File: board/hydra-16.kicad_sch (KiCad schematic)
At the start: 35 parts, among them J1 Conn_01x32, J2 Conn_01x24, J3 DE9_Plug, U1 74F573, U2 74F541, U3 AT28C64B, U4 W65C02SxP, U5 6522, U6 6551, U7 MAX232, U8 628512_DIP32, U9 74LS154

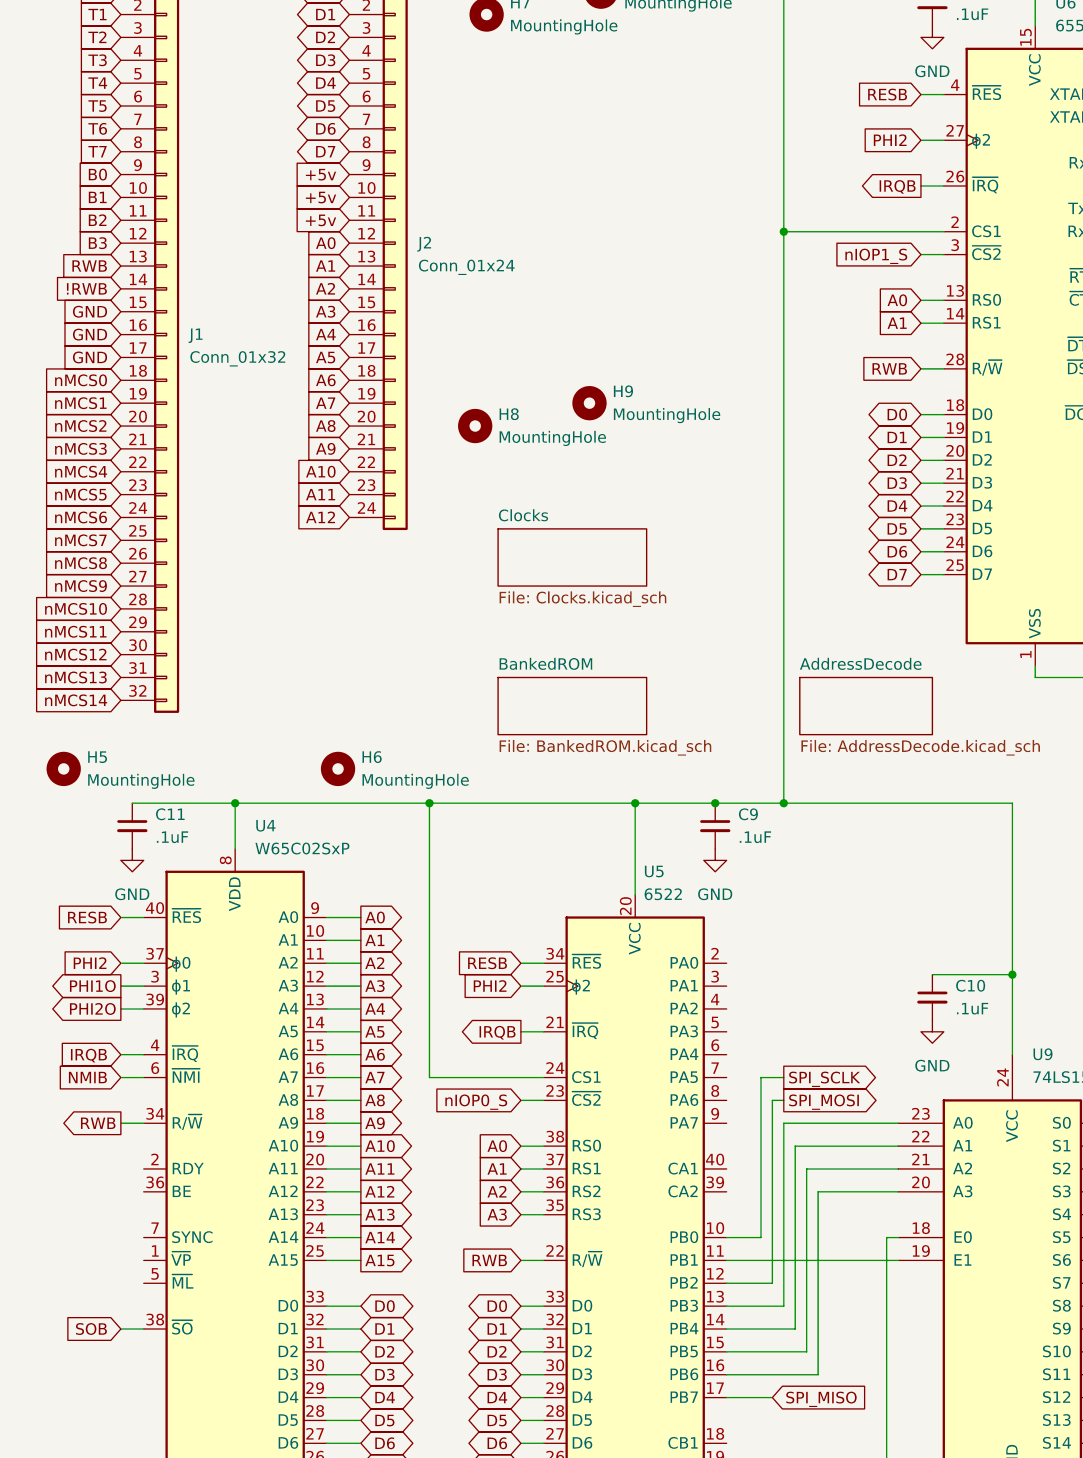
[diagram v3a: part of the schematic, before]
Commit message: Changing to ATX-sized motherboard with 8 62-pin ISA slots.  Other component connection cleanup as well.
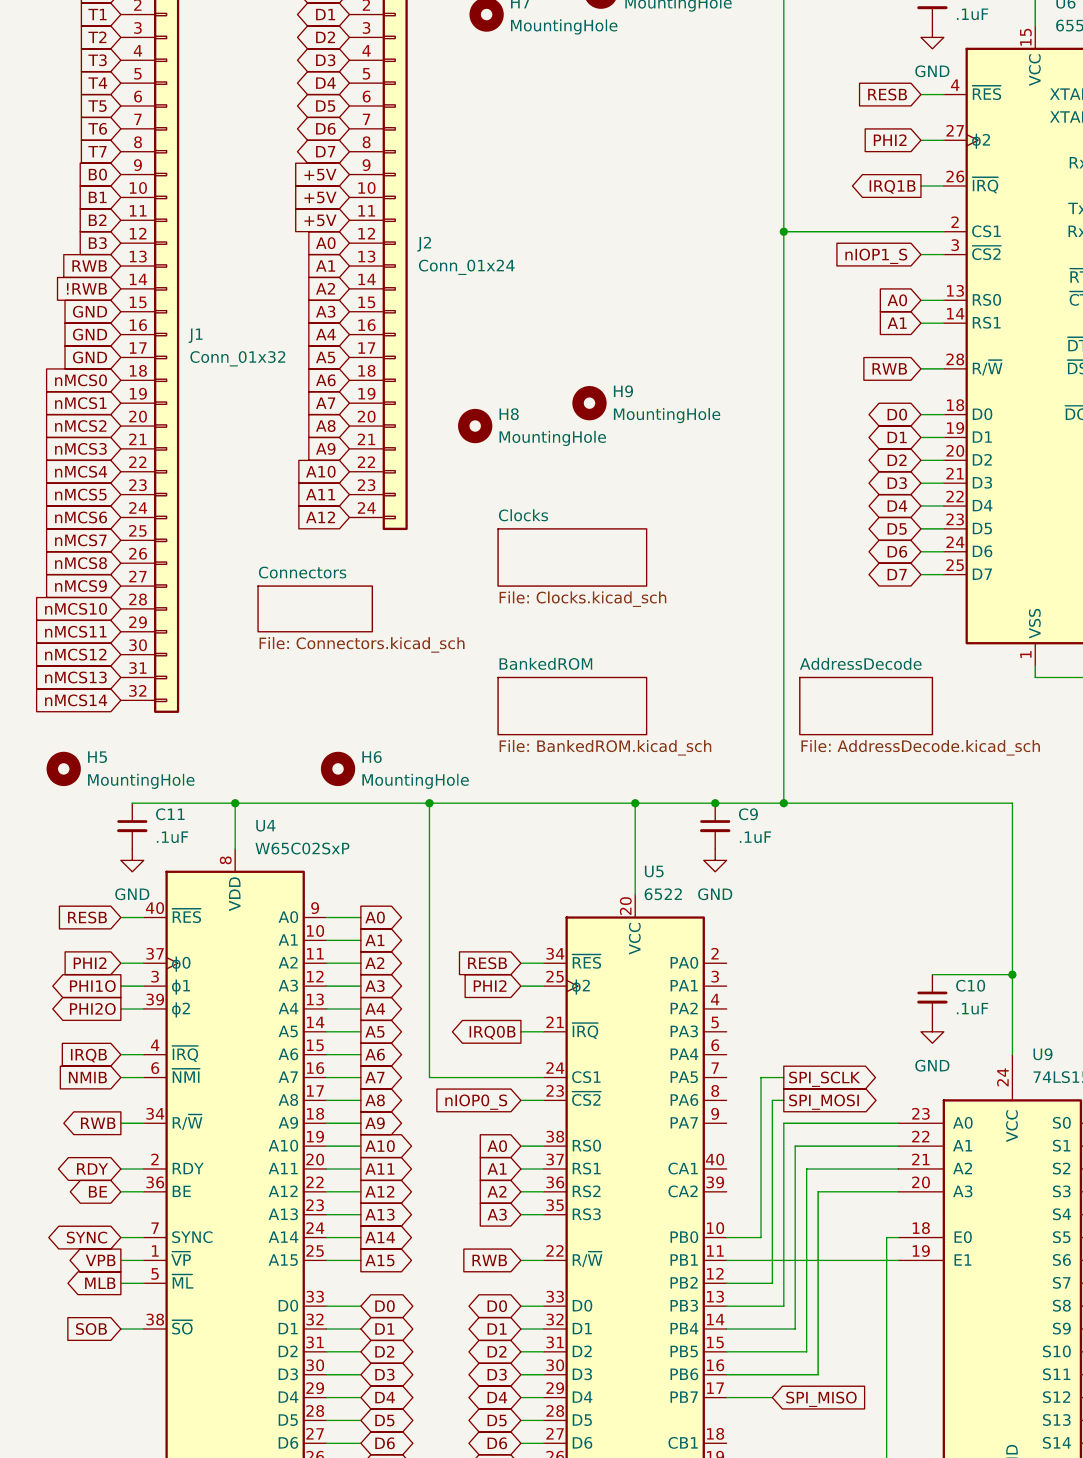
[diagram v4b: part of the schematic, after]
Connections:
- net +5v is gone; now on net +5V: J2.10 (Pin_10), J2.11 (Pin_11), J2.9 (Pin_9)
- net IRQB: no longer U5.21 (~{IRQ}), U6.26 (~{IRQ})
- net VPB: now reaches U4.1 (~{VP})
- net RDY: now reaches U4.2 (RDY)
- net BE: now reaches U4.36 (BE)
- net MLB: now reaches U4.5 (~{ML})
- net SYNC: now reaches U4.7 (SYNC)
- new net IRQ0B: U5.21 (~{IRQ})
- new net IRQ1B: U6.26 (~{IRQ})
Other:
- added sheet Connectors (Connectors.kicad_sch)
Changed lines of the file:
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@@
 	(wire
 		(pts
+			(xy 26.67 151.13) (xy 29.21 151.13)
+		)
+		(stroke
+			(width 0)
+			(type default)
+		)
+	)
+	(wire
+		(pts
 			(xy 274.32 124.46) (xy 273.05 124.46)
 		)
@@
 	(wire
 		(pts
+			(xy 26.67 158.75) (xy 29.21 158.75)
+		)
+		(stroke
+			(width 0)
+			(type default)
+		)
+	)
+	(wire
+		(pts
 			(xy 196.85 36.83) (xy 191.77 36.83)
 		)
@@
 	(wire
 		(pts
+			(xy 26.67 148.59) (xy 29.21 148.59)
+		)
+		(stroke
+			(width 0)
+			(type default)
+		)
+	)
+	(wire
+		(pts
 			(xy 246.38 19.05) (xy 246.38 16.51)
 		)
@@
 	(wire
 		(pts
+			(xy 26.67 156.21) (xy 29.21 156.21)
+		)
+		(stroke
+			(width 0)
+			(type default)
+		)
+	)
+	(wire
+		(pts
 			(xy 233.68 115.57) (xy 233.68 132.08)
 		)
@@
 	(wire
 		(pts
+			(xy 26.67 161.29) (xy 29.21 161.29)
+		)
+		(stroke
+			(width 0)
+			(type default)
+		)
+	)
+	(wire
+		(pts
 			(xy 176.53 44.45) (xy 190.5 44.45)
 		)
@@
 		)
 	)
+	(global_label "VPB"
+		(shape output)
+		(at 26.67 158.75 180)
+		(fields_autoplaced yes)
+		(effects
+			(font
+				(size 1.27 1.27)
+			)
+			(justify right)
+		)
+		(property "Intersheetrefs" "${INTERSHEET_REFS}"
+			(at 20.0562 158.75 0)
+			(effects
+				(font
+					(size 1.27 1.27)
+				)
+				(justify right)
+				(hide yes)
+			)
+		)
+	)
 	(global_label "A2"
 		(shape input)
@@
 		)
 	)
-	(global_label "IRQB"
+	(global_label "IRQ1B"
 		(shape output)
 		(at 115.57 39.37 180)
@@
 		)
 		(property "Intersheetrefs" "${INTERSHEET_REFS}"
-			(at 108.1095 39.37 0)
+			(at 106.9 39.37 0)
 			(effects
 				(font
@@
 		)
 	)
-	(global_label "+5v"
+	(global_label "+5V"
 		(shape input)
 		(at 52.07 40.64 180)
@@
 		)
 		(property "Intersheetrefs" "${INTERSHEET_REFS}"
-			(at 45.3353 40.64 0)
+			(at 45.2143 40.64 0)
 			(effects
 				(font
@@
 		)
 	)
+	(global_label "RDY"
+		(shape bidirectional)
+		(at 26.67 148.59 180)
+		(fields_autoplaced yes)
+		(effects
+			(font
+				(size 1.27 1.27)
+			)
+			(justify right)
+		)
+		(property "Intersheetrefs" "${INTERSHEET_REFS}"
+			(at 18.9449 148.59 0)
+			(effects
+				(font
+					(size 1.27 1.27)
+				)
+				(justify right)
+				(hide yes)
+			)
+		)
+	)
 	(global_label "A1"
 		(shape input)
@@
 		)
 	)
-	(global_label "+5v"
+	(global_label "+5V"
 		(shape input)
 		(at 52.07 38.1 180)
@@
 		)
 		(property "Intersheetrefs" "${INTERSHEET_REFS}"
-			(at 45.3353 38.1 0)
+			(at 45.2143 38.1 0)
 			(effects
 				(font
@@
 		)
 	)
+	(global_label "MLB"
+		(shape output)
+		(at 26.67 161.29 180)
+		(fields_autoplaced yes)
+		(effects
+			(font
+				(size 1.27 1.27)
+			)
+			(justify right)
+		)
+		(property "Intersheetrefs" "${INTERSHEET_REFS}"
+			(at 19.9353 161.29 0)
+			(effects
+				(font
+					(size 1.27 1.27)
+				)
+				(justify right)
+				(hide yes)
+			)
+		)
+	)
 	(global_label "SPI_CS6"
 		(shape output)
@@
 		)
 	)
-	(global_label "+5v"
+	(global_label "+5V"
 		(shape input)
 		(at 52.07 43.18 180)
@@
 		)
 		(property "Intersheetrefs" "${INTERSHEET_REFS}"
-			(at 45.3353 43.18 0)
+			(at 45.2143 43.18 0)
 			(effects
 				(font
@@
 		)
 	)
+	(global_label "SYNC"
+		(shape bidirectional)
+		(at 26.67 156.21 180)
+		(fields_autoplaced yes)
+		(effects
+			(font
+				(size 1.27 1.27)
+			)
+			(justify right)
+		)
+		(property "Intersheetrefs" "${INTERSHEET_REFS}"
+			(at 17.6749 156.21 0)
+			(effects
+				(font
+					(size 1.27 1.27)
+				)
+				(justify right)
+				(hide yes)
+			)
+		)
+	)
 	(global_label "nMCS12"
 		(shape input)
@@
 		)
 	)
+	(global_label "BE"
+		(shape bidirectional)
+		(at 26.67 151.13 180)
+		(fields_autoplaced yes)
+		(effects
+			(font
+				(size 1.27 1.27)
+			)
+			(justify right)
+		)
+		(property "Intersheetrefs" "${INTERSHEET_REFS}"
+			(at 20.1545 151.13 0)
+			(effects
+				(font
+					(size 1.27 1.27)
+				)
+				(justify right)
+				(hide yes)
+			)
+		)
+	)
 	(global_label "D6"
 		(shape tri_state)
@@
 		)
 	)
-	(global_label "IRQB"
+	(global_label "IRQ0B"
 		(shape output)
 		(at 71.12 133.35 180)
@@
 		)
 		(property "Intersheetrefs" "${INTERSHEET_REFS}"
-			(at 63.6595 133.35 0)
+			(at 62.45 133.35 0)
 			(effects
 				(font
@@
 				)
 			)
+		)
+	)
+	(sheet
+		(at 41.91 83.82)
+		(size 12.7 5.08)
+		(fields_autoplaced yes)
+		(stroke
+			(width 0.1524)
+			(type solid)
+		)
+		(fill
+			(color 0 0 0 0.0000)
+		)
+		(property "Sheetname" "Connectors"
+			(at 41.91 83.1084 0)
+			(effects
+				(font
+					(size 1.27 1.27)
+				)
+				(justify left bottom)
+			)
+		)
+		(property "Sheetfile" "Connectors.kicad_sch"
+			(at 41.91 89.4846 0)
+			(effects
+				(font
+					(size 1.27 1.27)
+				)
+				(justify left top)
+			)
+		)
+		(instances
+			(project "hydra-16"
+				(path "/ef29fc71-3fec-48b5-8a1a-46bee537a98c"
+					(page "7")
+				)
+			)

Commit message: Sample routed PCB with fills.  Not a final version, just an example
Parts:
- H1, H10, H2, H3, H4, H5, H6, H7, H8, H9: footprint MountingHole:MountingHole_3.2mm_M3 -> MountingHole:MountingHole_3.2mm_M3_Pad_TopBottom
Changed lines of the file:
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@@
 			)
 		)
-		(property "Footprint" "MountingHole:MountingHole_3.2mm_M3"
+		(property "Footprint" "MountingHole:MountingHole_3.2mm_M3_Pad_TopBottom"
 			(at 254 160.02 0)
 			(effects
@@
 			)
 		)
-		(property "Footprint" "MountingHole:MountingHole_3.2mm_M3"
+		(property "Footprint" "MountingHole:MountingHole_3.2mm_M3_Pad_TopBottom"
 			(at 78.74 63.5 0)
 			(effects
@@
 			)
 		)
-		(property "Footprint" "MountingHole:MountingHole_3.2mm_M3"
+		(property "Footprint" "MountingHole:MountingHole_3.2mm_M3_Pad_TopBottom"
 			(at 67.31 20.32 0)
 			(effects
@@
 			)
 		)
-		(property "Footprint" "MountingHole:MountingHole_3.2mm_M3"
+		(property "Footprint" "MountingHole:MountingHole_3.2mm_M3_Pad_TopBottom"
 			(at 198.12 160.02 0)
 			(effects
@@
 			)
 		)
-		(property "Footprint" "MountingHole:MountingHole_3.2mm_M3"
+		(property "Footprint" "MountingHole:MountingHole_3.2mm_M3_Pad_TopBottom"
 			(at 20.32 104.14 0)
 			(effects
@@
 			)
 		)
-		(property "Footprint" "MountingHole:MountingHole_3.2mm_M3"
+		(property "Footprint" "MountingHole:MountingHole_3.2mm_M3_Pad_TopBottom"
 			(at 80.01 17.78 0)
 			(effects
@@
 			)
 		)
-		(property "Footprint" "MountingHole:MountingHole_3.2mm_M3"
+		(property "Footprint" "MountingHole:MountingHole_3.2mm_M3_Pad_TopBottom"
 			(at 168.91 160.02 0)
 			(effects
@@
 			)
 		)
-		(property "Footprint" "MountingHole:MountingHole_3.2mm_M3"
+		(property "Footprint" "MountingHole:MountingHole_3.2mm_M3_Pad_TopBottom"
 			(at 226.06 160.02 0)
 			(effects
@@
 			)
 		)
-		(property "Footprint" "MountingHole:MountingHole_3.2mm_M3"
+		(property "Footprint" "MountingHole:MountingHole_3.2mm_M3_Pad_TopBottom"
 			(at 50.8 104.14 0)
 			(effects
@@
 			)
 		)
-		(property "Footprint" "MountingHole:MountingHole_3.2mm_M3"
+		(property "Footprint" "MountingHole:MountingHole_3.2mm_M3_Pad_TopBottom"
 			(at 66.04 66.04 0)
 			(effects

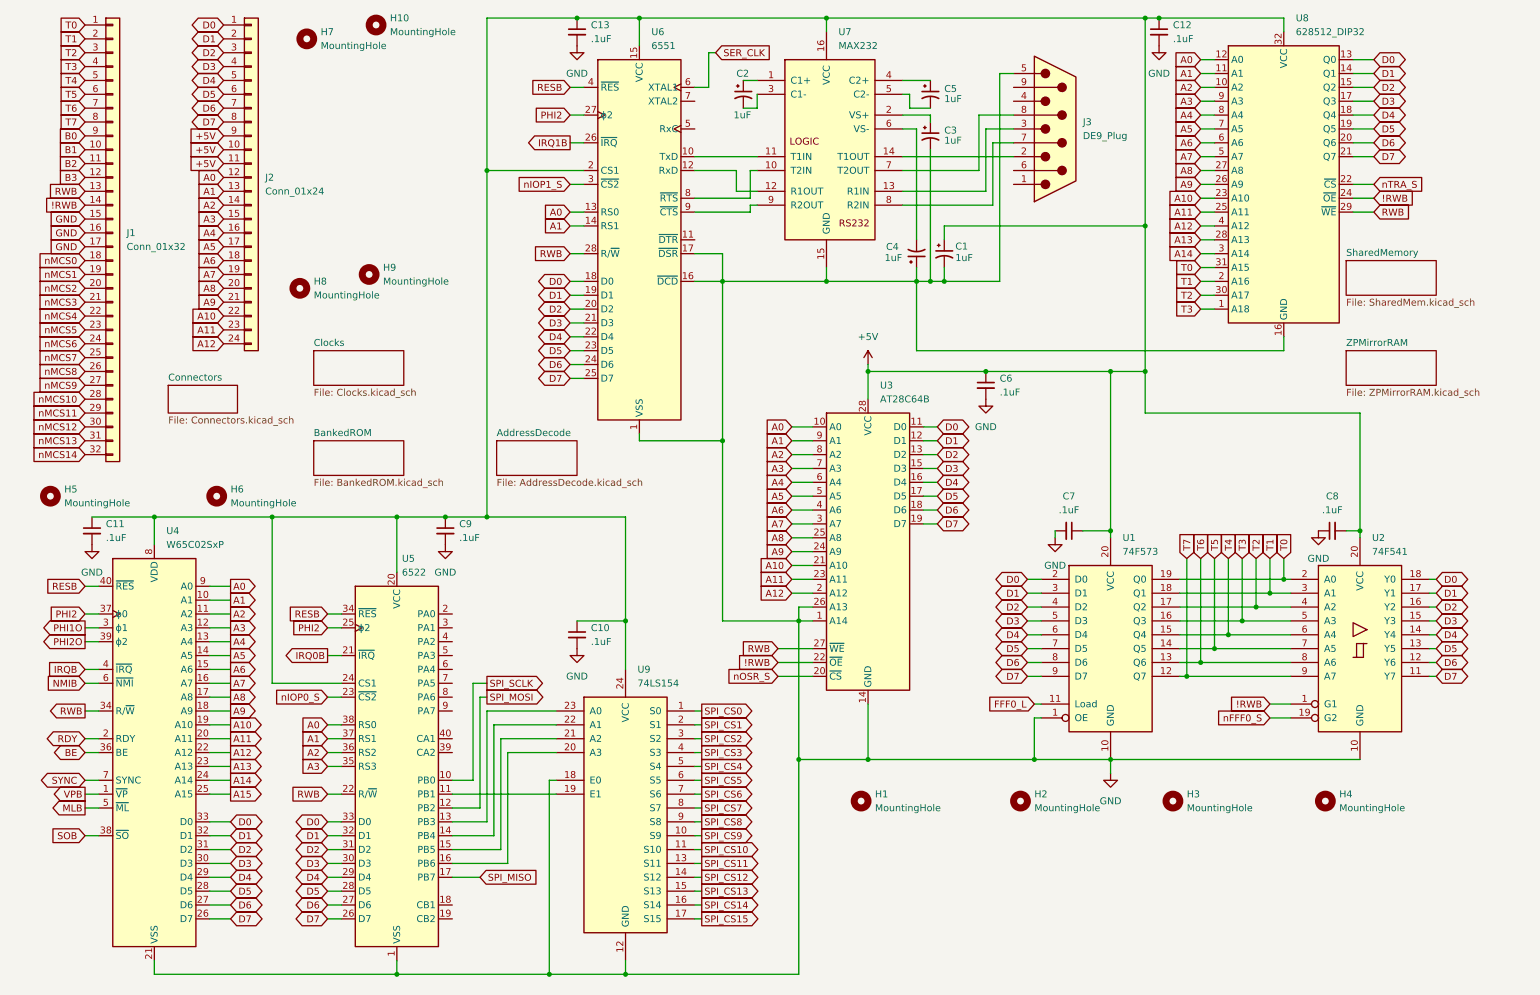
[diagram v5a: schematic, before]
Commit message: Added surface mount version of memory daughter cards, and lots of schematic updates and fixes, including adding dedicated registers for shared memory bank select at $FFF1 and IRQ vTable entry selector at $FFF2 along with the IRQ vTable registers and priority encoders for 16 IRQs
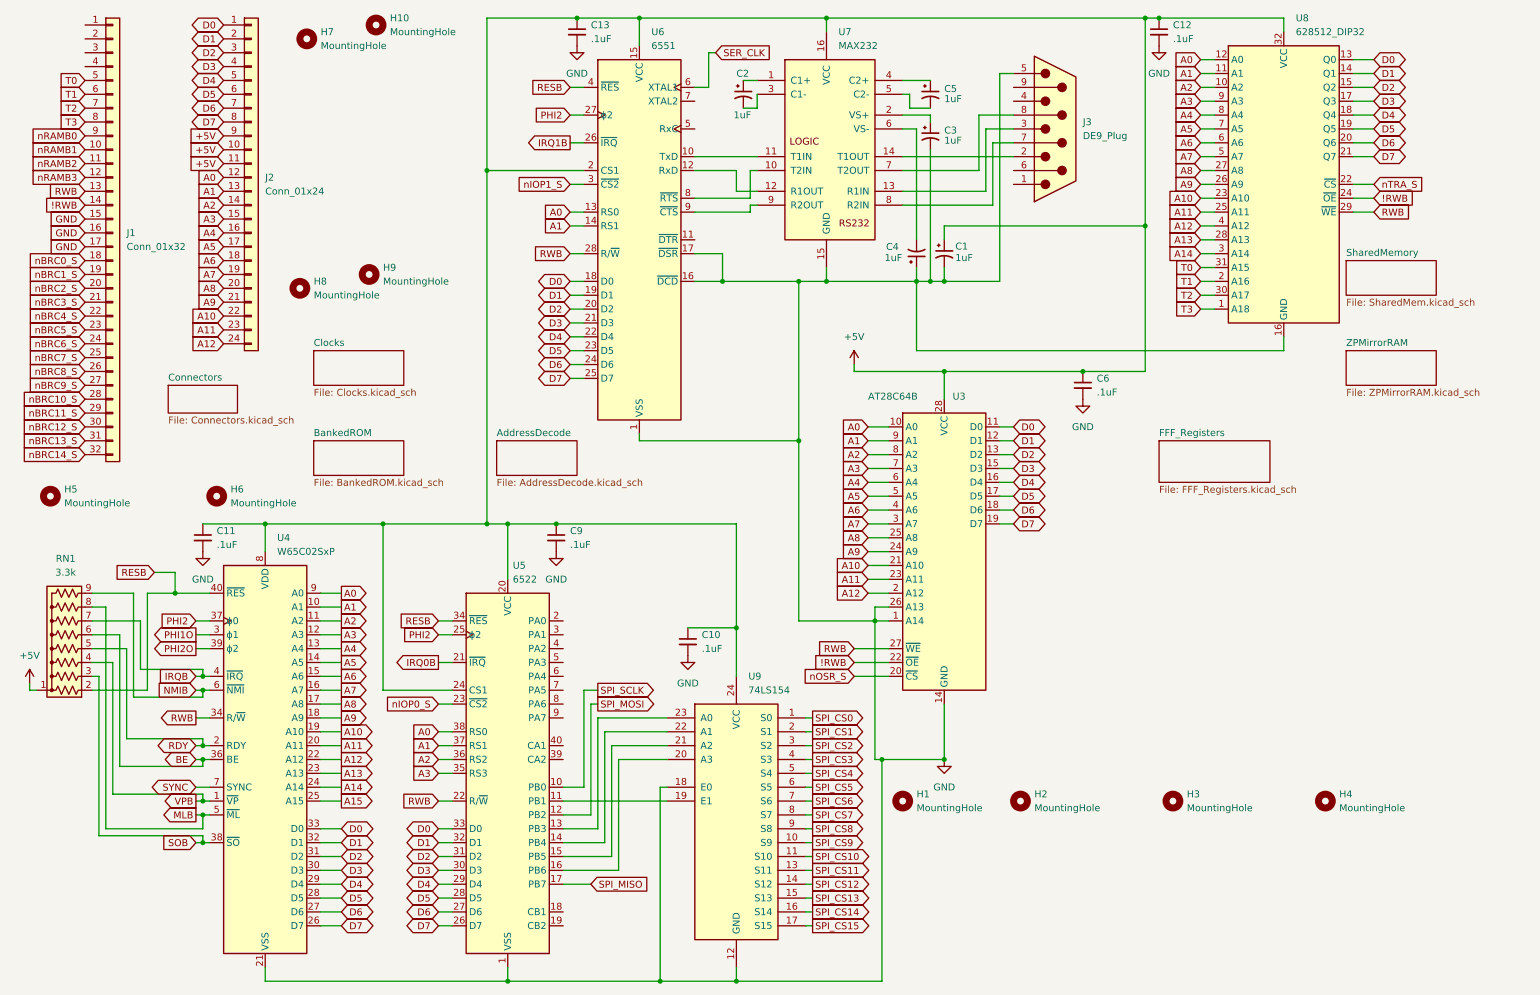
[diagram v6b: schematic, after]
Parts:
- removed C7, C8: .1uF, Capacitor_THT:C_Disc_D5.0mm_W2.5mm_P5.00mm, symbol Device:C_Small
- removed U1: 74F573, Package_DIP:DIP-20_W7.62mm_LongPads, symbol 74xx:74LS573
- removed U2: 74F541, Package_DIP:DIP-20_W7.62mm_LongPads, symbol 74xx:74LS541
- added RN1: 3.3k, Resistor_THT:R_Array_SIP9, symbol Device:R_Network08_US
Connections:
- net T4 is gone; now on net T0: J1.5 (Pin_5)
- net T5 is gone; now on net T1: J1.6 (Pin_6)
- net T6 is gone; now on net T2: J1.7 (Pin_7)
- net T7 is gone; now on net T3: J1.8 (Pin_8)
- net +5V: now also RN1.1 (common)
- net BE: now also RN1.6 (R5)
- net IRQB: now also RN1.7 (R6)
- net MLB: now also RN1.8 (R7)
- net NMIB: now also RN1.9 (R8)
- net RDY: now also RN1.5 (R4)
- net RESB: now also RN1.2 (R1)
- net SOB: now also RN1.3 (R2)
- net T0: no longer J1.1 (Pin_1)
- net T1: no longer J1.2 (Pin_2)
- net T2: no longer J1.3 (Pin_3)
- net T3: no longer J1.4 (Pin_4)
- net VPB: now also RN1.4 (R3)
- net B0 renamed nRAMB0
- net B1 renamed nRAMB1
- net B2 renamed nRAMB2
- net B3 renamed nRAMB3
- net nMCS0 renamed nBRC0_S
- net nMCS1 renamed nBRC1_S
- net nMCS10 renamed nBRC10_S
- net nMCS11 renamed nBRC11_S
- net nMCS12 renamed nBRC12_S
- net nMCS13 renamed nBRC13_S
- net nMCS14 renamed nBRC14_S
- net nMCS2 renamed nBRC2_S
- net nMCS3 renamed nBRC3_S
- net nMCS4 renamed nBRC4_S
- net nMCS5 renamed nBRC5_S
- net nMCS6 renamed nBRC6_S
- net nMCS7 renamed nBRC7_S
- net nMCS8 renamed nBRC8_S
- net nMCS9 renamed nBRC9_S
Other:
- added sheet FFF_Registers (FFF_Registers.kicad_sch)
- moved on the sheet: C10, C11, C6, C9, H1, U3, U4, U5, U9
